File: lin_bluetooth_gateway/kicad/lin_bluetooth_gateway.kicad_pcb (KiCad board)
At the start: 2 copper layers, 30.8 x 59.2 mm, 9 parts, among them P1 MOLEX-0431603103, P2 MOLEX-0431603103, P4 CONN_01X03, U1 MCP2050, U2 BL652

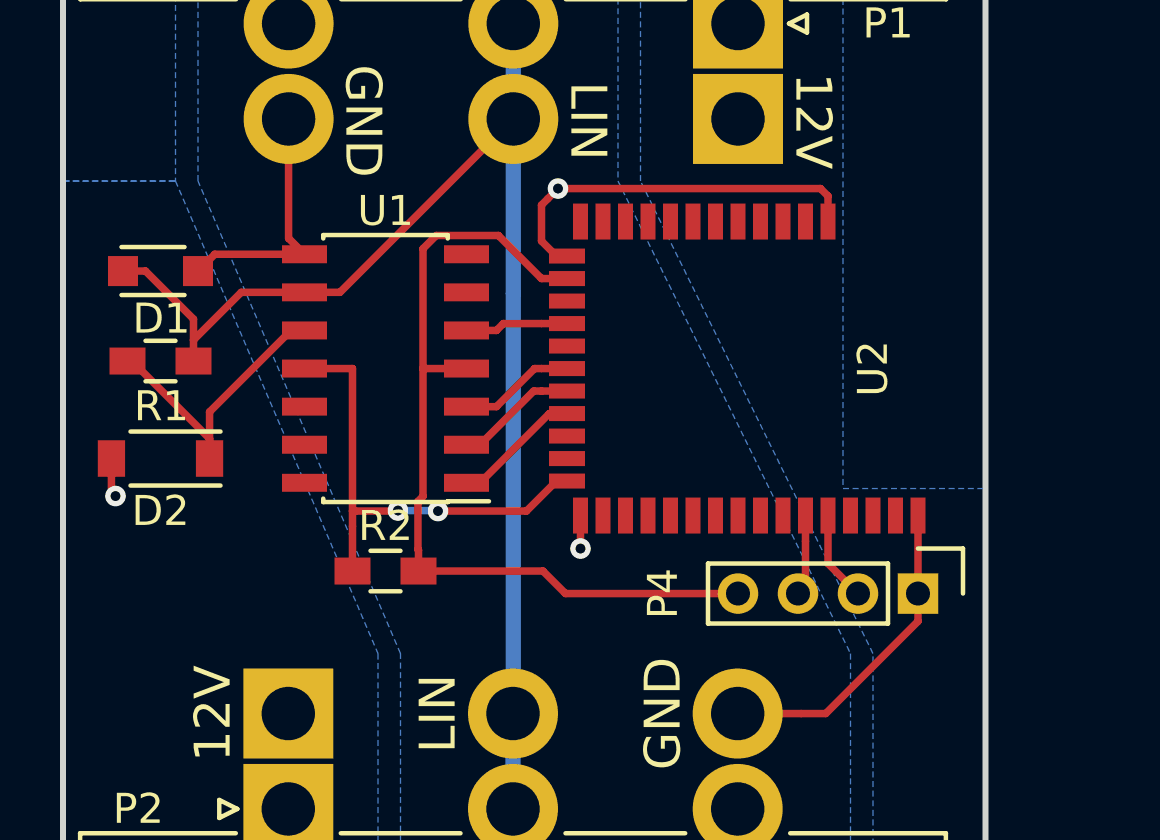
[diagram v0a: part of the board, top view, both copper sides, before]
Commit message: Refactoring directories
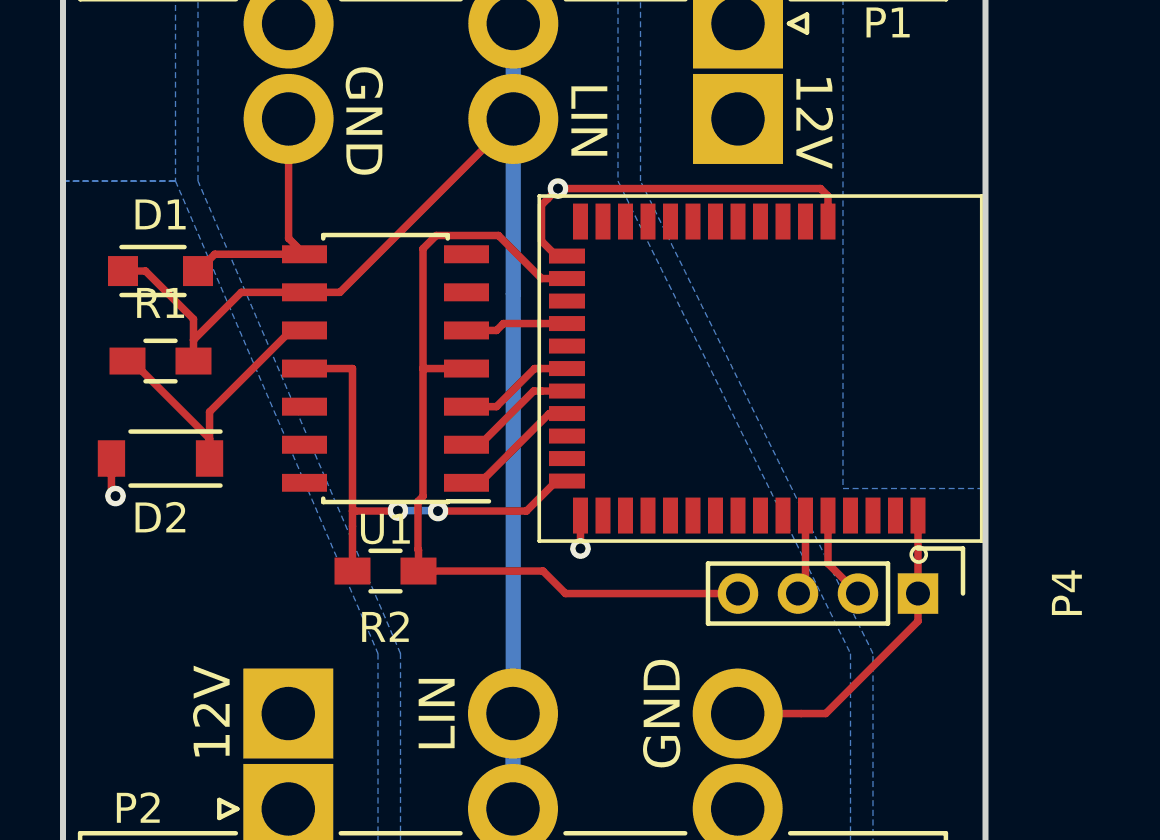
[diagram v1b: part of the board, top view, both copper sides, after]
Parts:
- D2: value D -> 1N4148
- U2: footprint footprints:BL652-SA -> Bluetooth_Modules:Bluetooth_Module_Laird_BL652
- moved U2 1.12 mm to (156.4, 102.5), turned to 180 degrees

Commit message: Using RF_Modules instead of Bluetooth_Modules for BL652
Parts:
- U2: footprint Bluetooth_Modules:Bluetooth_Module_Laird_BL652 -> RF_Modules:Laird_BL652

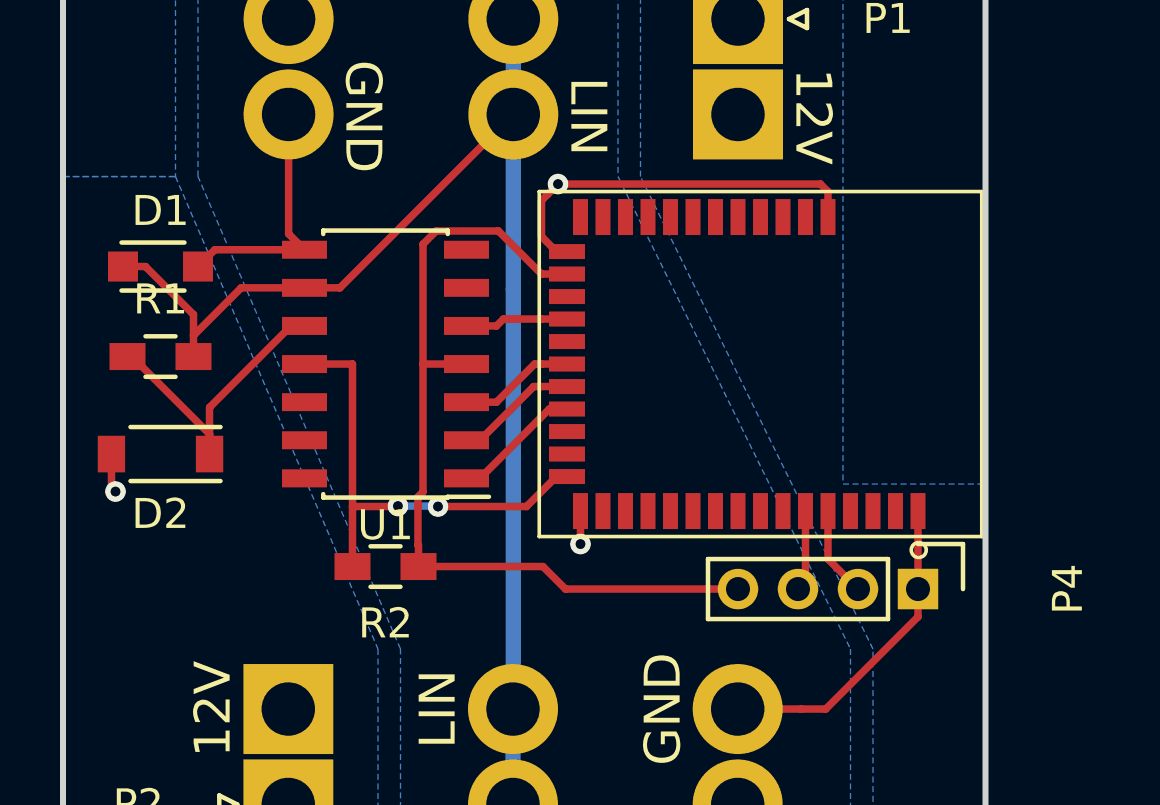
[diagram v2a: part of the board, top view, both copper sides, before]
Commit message: First working NRF52 master with two slave PIC nodes
# Software

* Using LIN 2.x checksum instead of LIN 1.x
* Using 19200 baudrate instead of 20000 for compatibility with NRF52
* Setting only the NRF52 as master
* Deactivating sleep mode for PIC as it was broken
* Ignoring break signal (not generated by NRF52 yet)
* Code cleaning: removing unused functions

# Boards

* Updating Git submodules
* Moving text references for the 8x input board
* Adding a TODO note for replacing the LIN pull-up resistor
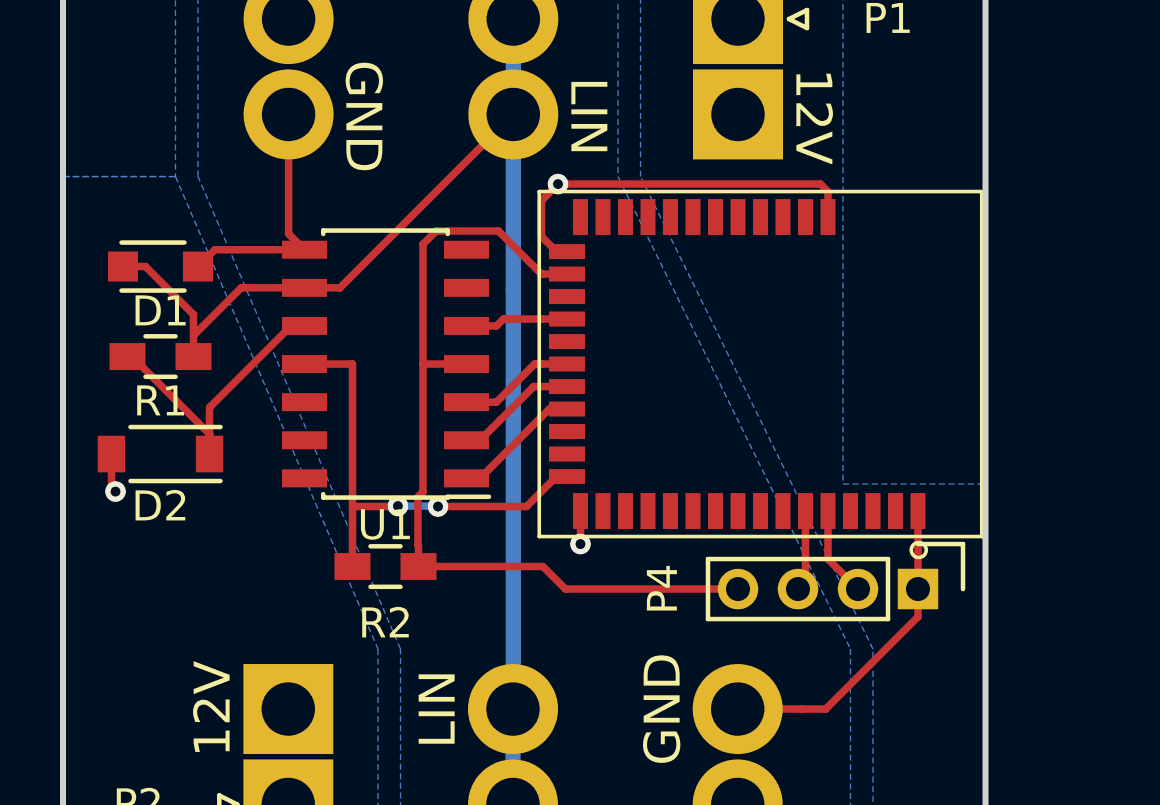
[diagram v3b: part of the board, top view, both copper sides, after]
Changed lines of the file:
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@@
-(kicad_pcb (version 4) (host pcbnew 4.0.4+e1-6308~48~ubuntu16.04.1-stable)
+(kicad_pcb (version 4) (host pcbnew 4.0.5-e0-6337~49~ubuntu16.04.1)
   (general
     (links 33)
@@
     (tags "resistor 0603")
     (attr smd)
-    (fp_text reference R1 (at 0 -1.9) (layer F.SilkS)
+    (fp_text reference R1 (at 0 1.5) (layer F.SilkS)
       (effects (font (size 1 1) (thickness 0.15)))
     )
@@
     (descr "Through hole pin header, 1x04, 2.00mm pitch, single row")
     (tags "pin header single row")
-    (fp_text reference P4 (at 0 -5 270) (layer F.SilkS)
+    (fp_text reference P4 (at 0 8.5 270) (layer F.SilkS)
       (effects (font (size 1 1) (thickness 0.15)))
     )
@@
     (tags SOD-123)
     (attr smd)
-    (fp_text reference D2 (at 0 -2 180) (layer F.SilkS)
+    (fp_text reference D2 (at 0 -1.75 180) (layer F.SilkS)
       (effects (font (size 1 1) (thickness 0.15)))
     )
@@
     (tags SOD-323)
     (attr smd)
-    (fp_text reference D1 (at 0 -1.85) (layer F.SilkS)
-      (effects (font (size 1 1) (thickness 0.15)))
-    )
+    (fp_text reference D1 (at 0 1.5) (layer F.SilkS)
+      (effects (font (size 1 1) (thickness 0.15)))
+    )
